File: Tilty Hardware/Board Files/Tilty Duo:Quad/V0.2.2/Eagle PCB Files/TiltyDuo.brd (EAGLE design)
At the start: 38.1 x 50.8 mm, 43 parts, among them U1 TEENSY_3.0_OUTER-PINS28-DIP_S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, U2 HC-09_BREAKOUT, U3 MPL3115A2LGA8, U4 LM2931, U5 MPU-6050, U6 HMC5883LSMD, U7 24LC08BT

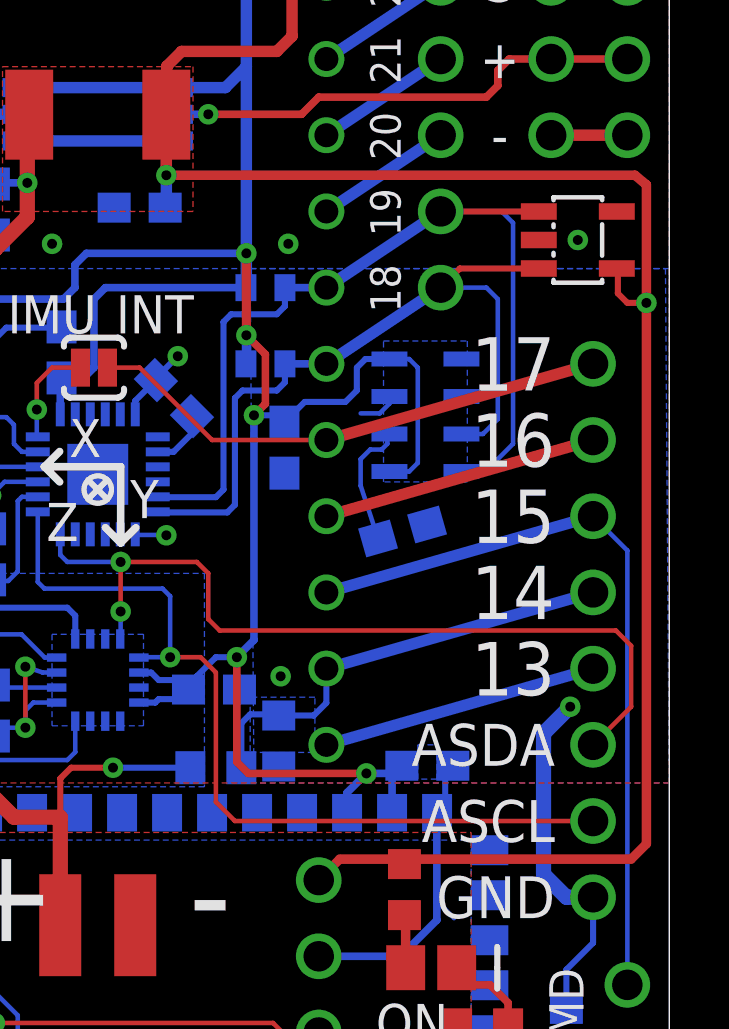
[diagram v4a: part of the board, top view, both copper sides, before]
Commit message: Fixed a problem on the prototype PCB and added EEPROM testing code
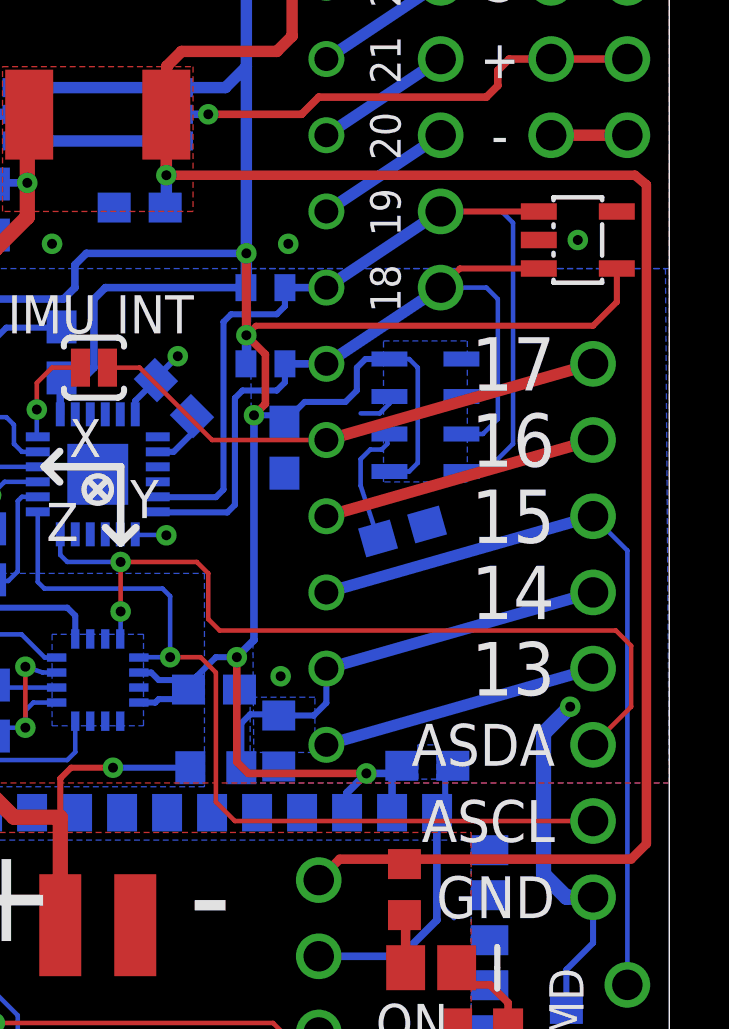
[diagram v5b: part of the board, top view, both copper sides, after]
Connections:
- net 5V: no longer U7.4
- net TEENSY_3V3: now also U7.4
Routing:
- net TEENSY_3V3: track 135.2 -> 149.1 mm
- net 5V: track 81.3 -> 79.4 mm, vias 2 -> 1
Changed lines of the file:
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@@
 <wire x1="27.9735" y1="29.2435" x2="27.686" y2="28.956" width="0.2032" layer="16"/>
 <wire x1="27.686" y1="28.956" x2="27.686" y2="28.194" width="0.2032" layer="16"/>
+<contactref element="U7" pad="4"/>
+<wire x1="36.352" y1="32.2605" x2="36.352" y2="31.145" width="0.2032" layer="1"/>
+<wire x1="36.352" y1="31.145" x2="35.56" y2="30.353" width="0.2032" layer="1"/>
+<wire x1="35.56" y1="30.353" x2="24.3205" y2="30.353" width="0.2032" layer="1"/>
+<wire x1="24.3205" y1="30.353" x2="24.003" y2="30.0355" width="0.2032" layer="1"/>
 </signal>
 <signal name="5V">
@@
 <contactref element="R4" pad="1"/>
 <contactref element="JP9" pad="4"/>
-<wire x1="37.338" y1="13.081" x2="37.338" y2="31.115" width="0.3175" layer="1"/>
-<via x="37.338" y="31.115" extent="1-16" drill="0.3302"/>
+<wire x1="37.338" y1="13.081" x2="37.338" y2="35.052" width="0.3175" layer="1"/>
 <wire x1="36.83" y1="12.573" x2="37.338" y2="13.081" width="0.3048" layer="1"/>
 <wire x1="27.1145" y1="12.573" x2="26.416" y2="11.8745" width="0.3048" layer="1"/>
-<contactref element="U7" pad="4"/>
 <wire x1="36.83" y1="12.573" x2="29.2735" y2="12.573" width="0.3175" layer="1"/>
 <wire x1="27.1145" y1="12.573" x2="29.2735" y2="12.573" width="0.3175" layer="1"/>
@@
 <wire x1="21.336" y1="34.329" x2="21.297" y2="34.29" width="0.381" layer="16"/>
 <wire x1="16.51" y1="36.5125" x2="21.59" y2="36.5125" width="0.381" layer="16"/>
-<wire x1="37.338" y1="31.115" x2="37.338" y2="35.052" width="0.3175" layer="1"/>
 <wire x1="37.338" y1="35.052" x2="36.957" y2="35.3695" width="0.3175" layer="1"/>
 <wire x1="36.957" y1="35.3695" x2="21.336" y2="35.3695" width="0.3175" layer="1"/>
-<wire x1="37.338" y1="31.115" x2="36.703" y2="31.115" width="0.2032" layer="1"/>
-<wire x1="36.703" y1="31.115" x2="36.3855" y2="31.4325" width="0.2032" layer="1"/>
-<wire x1="36.3855" y1="31.4325" x2="36.3855" y2="32.227" width="0.2032" layer="1"/>
-<wire x1="36.3855" y1="32.227" x2="36.352" y2="32.2605" width="0.2032" layer="1"/>
 <wire x1="21.3487" y1="37.4015" x2="21.3487" y2="39.0017" width="0.381" layer="1"/>
 <wire x1="21.3487" y1="39.0017" x2="21.844" y2="39.497" width="0.381" layer="1"/>
@@
 </signal>
 </signals>
-<errors>
-</errors>
 </board>
 </drawing>
